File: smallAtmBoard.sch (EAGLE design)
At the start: 25 parts, among them IC1 ATMEGA-328P, IC2 7805-V, Y1 16MHz

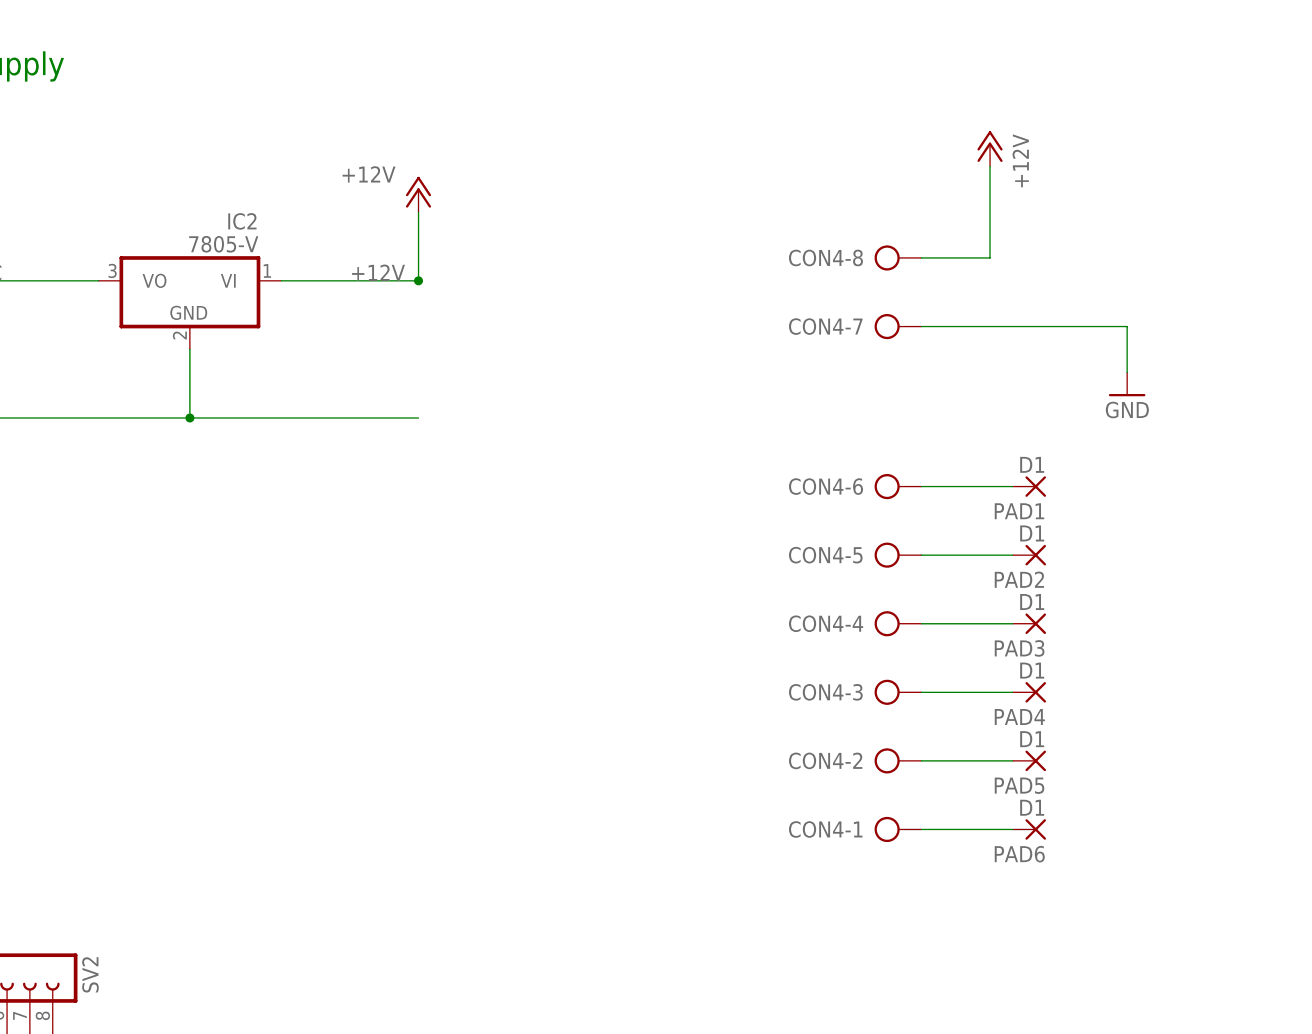
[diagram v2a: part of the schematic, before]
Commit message: move 7805 and change connector
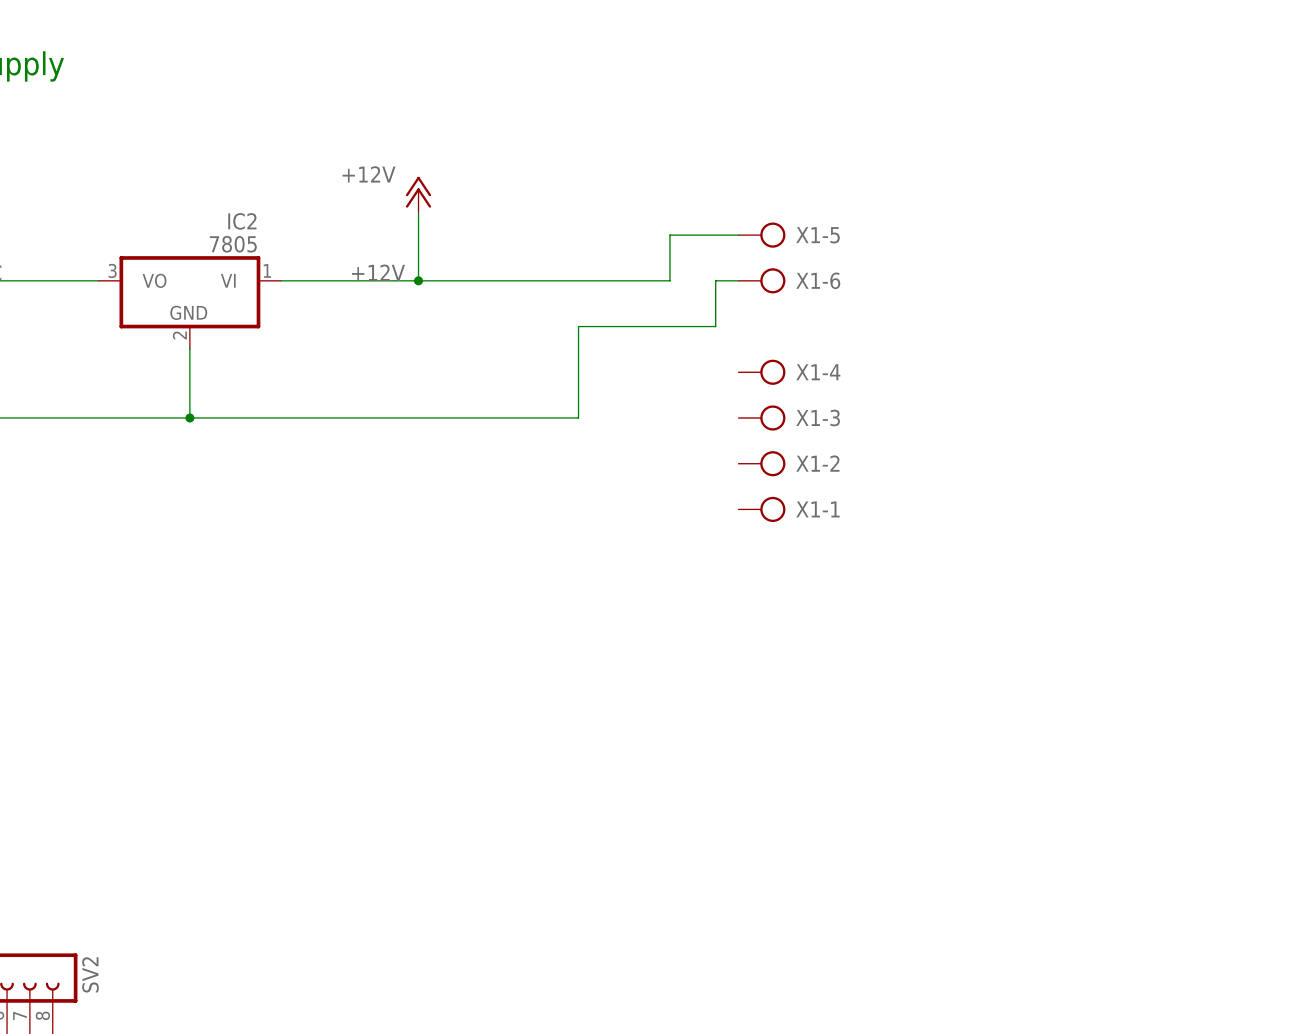
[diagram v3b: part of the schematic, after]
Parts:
- removed CON4: (no value), bauteile_jbt:AK300/8
- removed PAD1, PAD2, PAD3, PAD4, PAD5, PAD6: D1, bauteile_jbt:PAD1,6/0,8
- added X1: (no value), bauteile_jbt:AK300/6
- IC2: value 7805-V -> 7805
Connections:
- removed net N$21: CON4-6.KL, PAD1.P
- removed net N$22: CON4-5.KL, PAD2.P
- removed net N$23: CON4-4.KL, PAD3.P
- removed net N$24: CON4-3.KL, PAD4.P
- removed net N$25: CON4-2.KL, PAD5.P
- removed net N$26: CON4-1.KL, PAD6.P
- net +12V: now also X1-5.KL; no longer CON4-8.KL
- net GND: now also X1-6.KL; no longer CON4-7.KL
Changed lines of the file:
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@@
 <part name="C2" library="bauteile_jbt" deviceset="C-5" device="5MM" value="100n"/>
 <part name="R3" library="bauteile_jbt" deviceset="R-EU_" device="0207/2V" value="10k"/>
-<part name="CON4" library="bauteile_jbt" deviceset="AK300/8" device=""/>
 <part name="C4" library="bauteile_jbt" deviceset="C-5" device="5MM" value="22p"/>
 <part name="C5" library="bauteile_jbt" deviceset="C-5" device="5MM" value="22p"/>
-<part name="+12V1" library="supply1" deviceset="+12V" device=""/>
-<part name="GND15" library="supply1" deviceset="GND" device=""/>
 <part name="R16" library="bauteile_jbt" deviceset="R-EU_" device="0207/2V" value="330"/>
 <part name="GND17" library="supply1" deviceset="GND" device=""/>
@@
 <part name="+5V" library="supply1" deviceset="VCC" device=""/>
 <part name="+12V" library="supply1" deviceset="+12V" device=""/>
-<part name="IC2" library="bauteile_jbt" deviceset="7805" device="-V"/>
+<part name="IC2" library="bauteile_jbt" deviceset="7805" device="-V" value="7805"/>
 <part name="GND9" library="supply1" deviceset="GND" device=""/>
 <part name="R22" library="bauteile_jbt" deviceset="R-EU_" device="0207/2V" value="2.2k"/>
@@
 <part name="GND5" library="supply1" deviceset="GND" device=""/>
 <part name="GND6" library="supply1" deviceset="GND" device=""/>
-<part name="PAD1" library="bauteile_jbt" deviceset="PAD1,6/0,8" device="" value="D1"/>
-<part name="PAD2" library="bauteile_jbt" deviceset="PAD1,6/0,8" device="" value="D1"/>
-<part name="PAD3" library="bauteile_jbt" deviceset="PAD1,6/0,8" device="" value="D1"/>
-<part name="PAD4" library="bauteile_jbt" deviceset="PAD1,6/0,8" device="" value="D1"/>
-<part name="PAD5" library="bauteile_jbt" deviceset="PAD1,6/0,8" device="" value="D1"/>
-<part name="PAD6" library="bauteile_jbt" deviceset="PAD1,6/0,8" device="" value="D1"/>
 <part name="SV2" library="bauteile_jbt" deviceset="FE08-1" device="FE08-RAW"/>
 <part name="U$2" library="bauteile_jbt" deviceset="FE02-2" device=""/>
 <part name="P+1" library="supply1" deviceset="VCC" device=""/>
+<part name="X1" library="bauteile_jbt" deviceset="AK300/6" device=""/>
 </parts>
 <sheets>
@@
 <instance part="IC2" gate="G$1" x="210.82" y="218.44" rot="MR0"/>
 <instance part="GND9" gate="1" x="180.34" y="195.58"/>
-<instance part="CON4" gate="-1" x="287.02" y="157.48" rot="MR180"/>
-<instance part="CON4" gate="-2" x="287.02" y="165.1" rot="MR180"/>
-<instance part="CON4" gate="-3" x="287.02" y="172.72" rot="MR180"/>
-<instance part="CON4" gate="-4" x="287.02" y="180.34" rot="MR180"/>
-<instance part="CON4" gate="-5" x="287.02" y="187.96" rot="MR180"/>
-<instance part="CON4" gate="-6" x="287.02" y="195.58" rot="MR180"/>
-<instance part="CON4" gate="-7" x="287.02" y="213.36" rot="MR180"/>
-<instance part="CON4" gate="-8" x="287.02" y="220.98" rot="MR180"/>
-<instance part="+12V1" gate="1" x="299.72" y="233.68" rot="MR0"/>
-<instance part="GND15" gate="1" x="314.96" y="205.74" rot="MR0"/>
 <instance part="R22" gate="G$1" x="256.54" y="81.28" rot="R90"/>
 <instance part="R23" gate="G$1" x="266.7" y="99.06" rot="R90"/>
@@
 <instance part="GND5" gate="1" x="368.3" y="73.66"/>
 <instance part="GND6" gate="1" x="289.56" y="60.96"/>
-<instance part="PAD1" gate="P" x="304.8" y="195.58" rot="R180"/>
-<instance part="PAD2" gate="P" x="304.8" y="187.96" rot="R180"/>
-<instance part="PAD3" gate="P" x="304.8" y="180.34" rot="R180"/>
-<instance part="PAD4" gate="P" x="304.8" y="172.72" rot="R180"/>
-<instance part="PAD5" gate="P" x="304.8" y="165.1" rot="R180"/>
-<instance part="PAD6" gate="P" x="304.8" y="157.48" rot="R180"/>
 <instance part="SV2" gate="G$1" x="185.42" y="142.24" rot="R270"/>
 <instance part="U$2" gate="G$1" x="287.02" y="81.28" rot="R90"/>
@@
 <attribute name="VALUE" x="291.465" y="116.84" size="1.778" layer="96" rot="R180"/>
 </instance>
+<instance part="X1" gate="-1" x="276.86" y="193.04" rot="R180"/>
+<instance part="X1" gate="-2" x="276.86" y="198.12" rot="R180"/>
+<instance part="X1" gate="-3" x="276.86" y="203.2" rot="R180"/>
+<instance part="X1" gate="-4" x="276.86" y="208.28" rot="R180"/>
+<instance part="X1" gate="-5" x="276.86" y="223.52" rot="R180"/>
+<instance part="X1" gate="-6" x="276.86" y="218.44" rot="R180"/>
 </instances>
 <busses>
@@
 </segment>
 <segment>
-<wire x1="236.22" y1="203.2" x2="210.82" y2="203.2" width="0.1524" layer="91"/>
+<wire x1="254" y1="203.2" x2="210.82" y2="203.2" width="0.1524" layer="91"/>
 <wire x1="210.82" y1="203.2" x2="180.34" y2="203.2" width="0.1524" layer="91"/>
 <pinref part="IC2" gate="G$1" pin="GND"/>
@@
 <pinref part="GND9" gate="1" pin="GND"/>
 <junction x="210.82" y="203.2"/>
-</segment>
-<segment>
-<pinref part="CON4" gate="-7" pin="KL"/>
-<wire x1="292.1" y1="213.36" x2="314.96" y2="213.36" width="0.1524" layer="91"/>
-<wire x1="314.96" y1="213.36" x2="314.96" y2="208.28" width="0.1524" layer="91"/>
-<pinref part="GND15" gate="1" pin="GND"/>
+<wire x1="254" y1="203.2" x2="254" y2="213.36" width="0.1524" layer="91"/>
+<wire x1="254" y1="213.36" x2="269.24" y2="213.36" width="0.1524" layer="91"/>
+<wire x1="269.24" y1="213.36" x2="269.24" y2="218.44" width="0.1524" layer="91"/>
+<pinref part="X1" gate="-6" pin="KL"/>
+<wire x1="269.24" y1="218.44" x2="271.78" y2="218.44" width="0.1524" layer="91"/>
 </segment>
 <segment>
@@
 <wire x1="220.98" y1="218.44" x2="236.22" y2="218.44" width="0.1524" layer="91"/>
 <junction x="236.22" y="218.44"/>
-</segment>
-<segment>
-<pinref part="CON4" gate="-8" pin="KL"/>
-<wire x1="292.1" y1="220.98" x2="299.72" y2="220.98" width="0.1524" layer="91"/>
-<pinref part="+12V1" gate="1" pin="+12V"/>
-<wire x1="299.72" y1="220.98" x2="299.72" y2="231.14" width="0.1524" layer="91"/>
-</segment>
-</net>
-<net name="N$21" class="0">
-<segment>
-<pinref part="CON4" gate="-6" pin="KL"/>
-<pinref part="PAD1" gate="P" pin="P"/>
-<wire x1="292.1" y1="195.58" x2="302.26" y2="195.58" width="0.1524" layer="91"/>
-</segment>
-</net>
-<net name="N$22" class="0">
-<segment>
-<pinref part="CON4" gate="-5" pin="KL"/>
-<pinref part="PAD2" gate="P" pin="P"/>
-<wire x1="292.1" y1="187.96" x2="302.26" y2="187.96" width="0.1524" layer="91"/>
-</segment>
-</net>
-<net name="N$23" class="0">
-<segment>
-<pinref part="CON4" gate="-4" pin="KL"/>
-<pinref part="PAD3" gate="P" pin="P"/>
-<wire x1="292.1" y1="180.34" x2="302.26" y2="180.34" width="0.1524" layer="91"/>
-</segment>
-</net>
-<net name="N$24" class="0">
-<segment>
-<pinref part="CON4" gate="-3" pin="KL"/>
-<pinref part="PAD4" gate="P" pin="P"/>
-<wire x1="292.1" y1="172.72" x2="302.26" y2="172.72" width="0.1524" layer="91"/>
-</segment>
-</net>
-<net name="N$25" class="0">
-<segment>
-<pinref part="CON4" gate="-2" pin="KL"/>
-<pinref part="PAD5" gate="P" pin="P"/>
-<wire x1="292.1" y1="165.1" x2="302.26" y2="165.1" width="0.1524" layer="91"/>
-</segment>
-</net>
-<net name="N$26" class="0">
-<segment>
-<pinref part="CON4" gate="-1" pin="KL"/>
-<pinref part="PAD6" gate="P" pin="P"/>
-<wire x1="292.1" y1="157.48" x2="302.26" y2="157.48" width="0.1524" layer="91"/>
-</segment>
-</net>
+<wire x1="236.22" y1="218.44" x2="264.16" y2="218.44" width="0.1524" layer="91"/>
+<wire x1="264.16" y1="218.44" x2="264.16" y2="223.52" width="0.1524" layer="91"/>
+<pinref part="X1" gate="-5" pin="KL"/>
+<wire x1="264.16" y1="223.52" x2="271.78" y2="223.52" width="0.1524" layer="91"/>
+</segment>
+</net>
